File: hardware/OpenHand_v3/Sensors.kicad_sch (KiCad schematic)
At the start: 66 parts, among them U5 TL084, U6 TL084

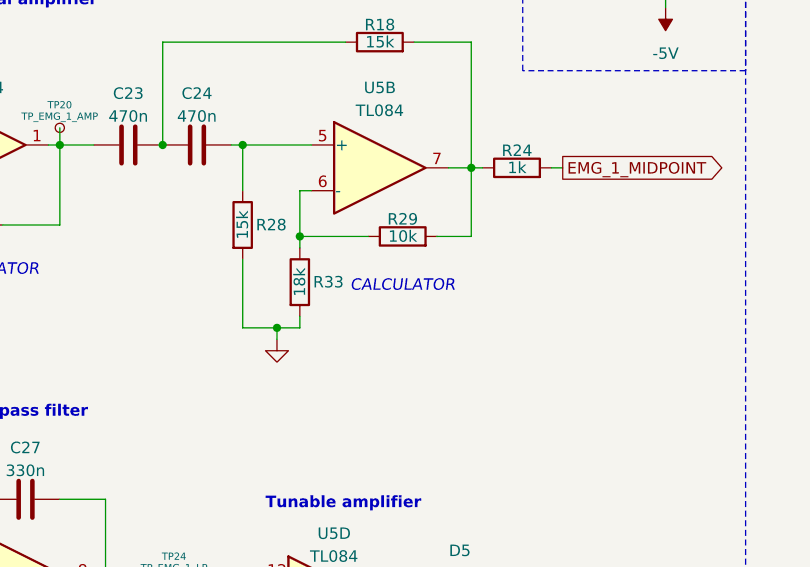
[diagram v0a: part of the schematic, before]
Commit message: Finalize board v3, prepare CubeIDE config
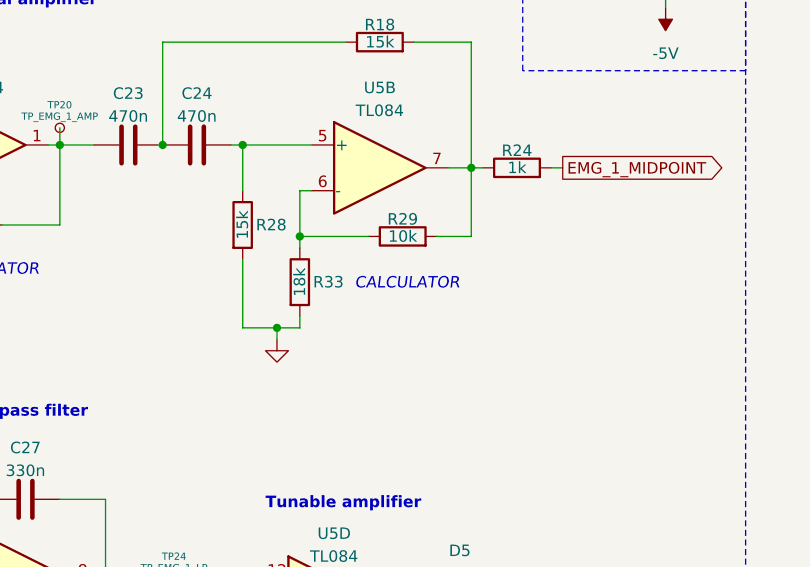
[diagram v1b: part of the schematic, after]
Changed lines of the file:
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@@
 	(text "CALCULATOR"
 		(exclude_from_sim no)
-		(at 106.68 72.898 0)
+		(at 107.188 72.644 0)
 		(effects
 			(font

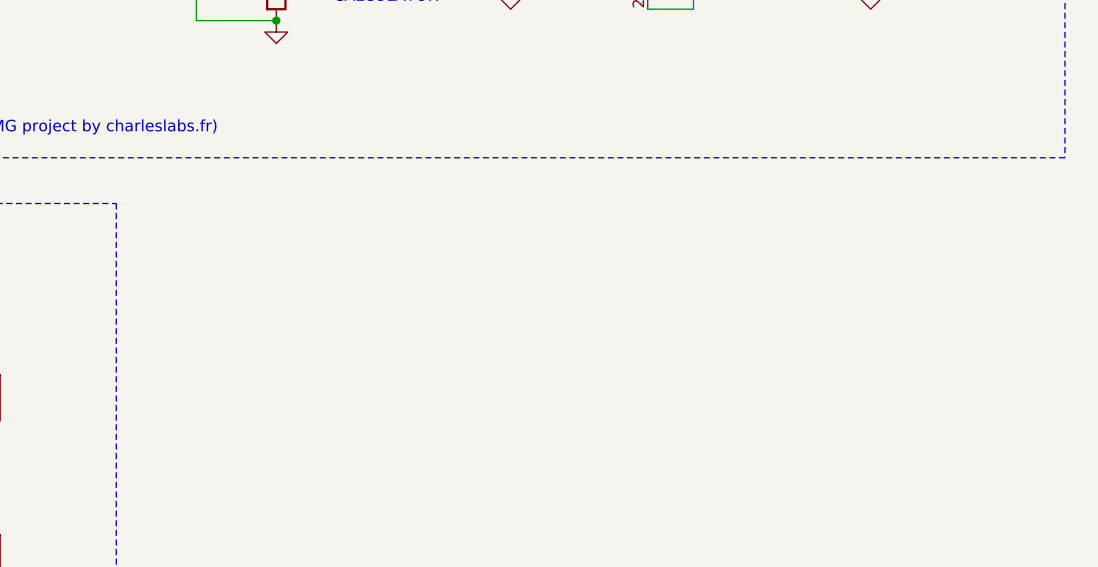
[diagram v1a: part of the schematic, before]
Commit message: Update PCB via size, start with code infrastructure idea
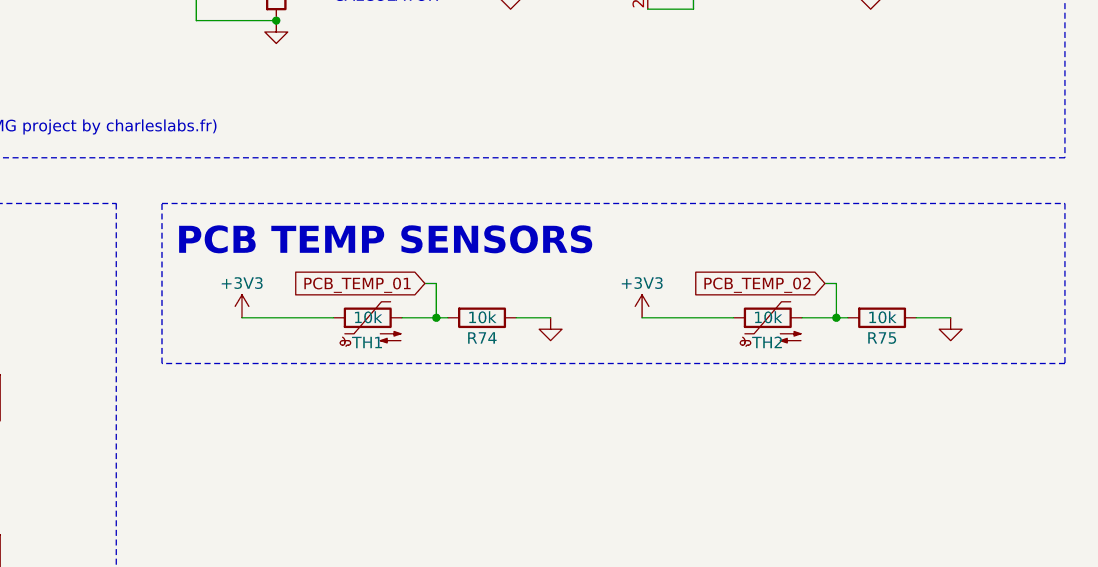
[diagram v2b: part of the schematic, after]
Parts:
- added R74, R75: 10k, Resistor_SMD:R_0805_2012Metric, symbol Device:R
- added TH1, TH2: 10k, Resistor_SMD:R_0805_2012Metric, symbol Device:Thermistor_NTC
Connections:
- net GND: now also R74.1, R75.1
- new net +3V3: TH1.1, TH2.1
- new net PCB_TEMP_01: R74.2, TH1.2
- new net PCB_TEMP_02: R75.2, TH2.2
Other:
- note added: "PCB TEMP SENSORS"
